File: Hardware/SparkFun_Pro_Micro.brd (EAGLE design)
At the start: 17.8 x 33 mm, 105 parts, among them J2 Qwiic, U1 3.3V, U3 ATmega32U4, Y2 16MHz

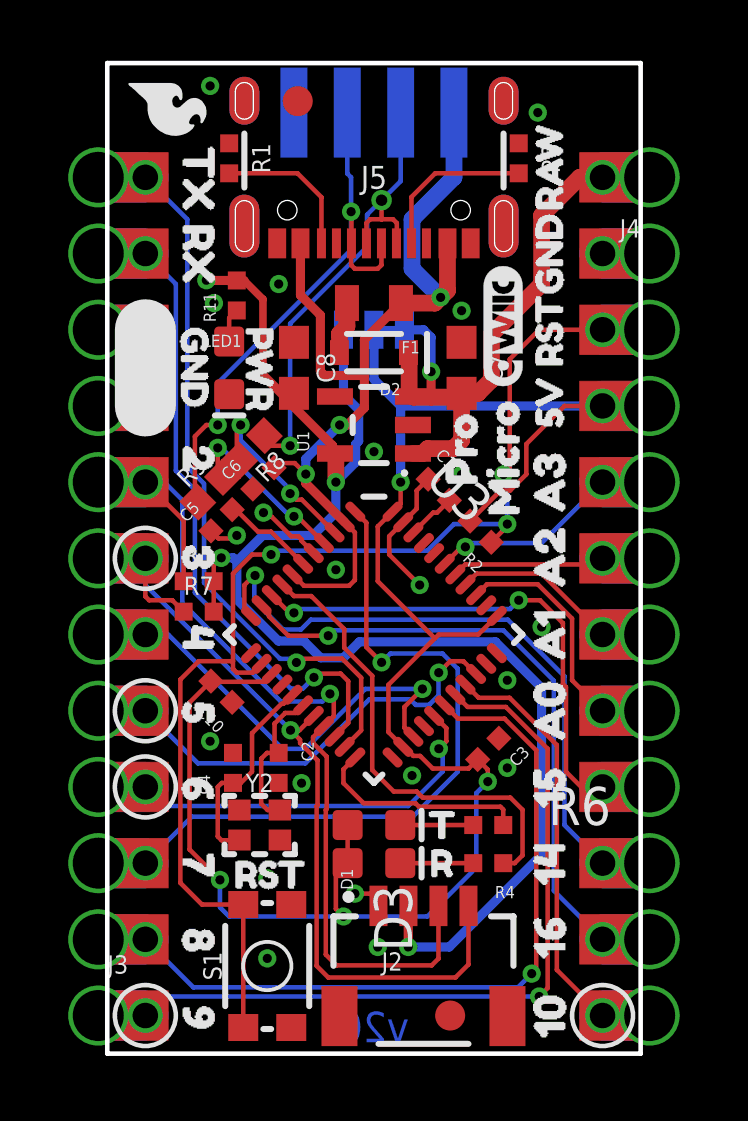
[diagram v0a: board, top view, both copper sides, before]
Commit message: fixing paste issue
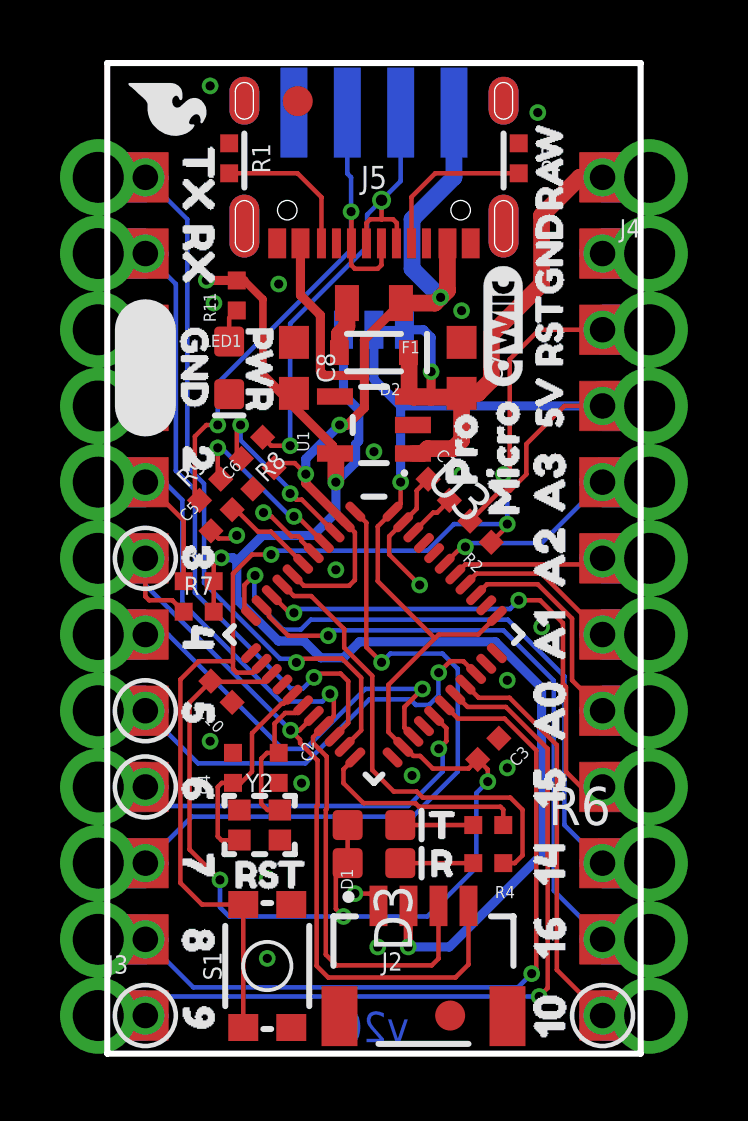
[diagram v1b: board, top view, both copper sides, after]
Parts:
- J2: value Qwiic -> QWIIC_RIGHT_ANGLE
- JP4: value (none) -> JUMPER-SMT_3_1-NC_TRACE_SILK
- R8, R9: value 22 -> 5.1k; device SparkFun-Resistors:0402 -> SparkFun-Resistors:0402-TIGHT
- U3: value ATmega32U4 -> 32U4; device SparkFun-IC-Microcontroller:QFN-44-NOPAD_1:1 -> SparkFun-IC-Microcontroller:QFN-44-NOPAD_1:1-LESS_PASTE
- moved U$32 2.90 mm to (14.7, 24.4), turned to 90 degrees
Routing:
- net RAW: track 19.5 -> 20.4 mm

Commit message: changing PROD_ID on series D+/D- resistor to proper PROD_ID
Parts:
- R8, R9: value 5.1k -> 22OHM-0402T-1/16W-1%
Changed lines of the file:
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@@
 <attribute name="VALUE" x="8.89" y="1.624" size="0.6096" layer="27" font="vector" ratio="20"/>
 </element>
-<element name="R8" library="SparkFun-Resistors" package="0402-TIGHT" value="5.1k" x="4.826" y="20.193" smashed="yes" rot="R225">
+<element name="R8" library="SparkFun-Resistors" package="0402-TIGHT" value="22OHM-0402T-1/16W-1%" x="4.826" y="20.193" smashed="yes" rot="R225">
 <attribute name="NAME" x="5.223396875" y="19.79560625" size="0.6096" layer="25" font="vector" ratio="20" rot="R225" align="bottom-center"/>
-<attribute name="PROD_ID" value="RES-14340" x="4.826" y="20.193" size="1.778" layer="27" font="vector" ratio="15" rot="R225" display="off"/>
-<attribute name="VALUE" value="5.1k" x="4.42860625" y="20.590396875" size="0.6096" layer="27" font="vector" ratio="20" rot="R225" align="top-center"/>
+<attribute name="PROD_ID" value="RES-12427" x="4.826" y="20.193" size="1.778" layer="27" font="vector" ratio="15" rot="R225" display="off"/>
 </element>
-<element name="R9" library="SparkFun-Resistors" package="0402-TIGHT" value="5.1k" x="3.429" y="18.796" smashed="yes" rot="R45">
+<element name="R9" library="SparkFun-Resistors" package="0402-TIGHT" value="22OHM-0402T-1/16W-1%" x="3.429" y="18.796" smashed="yes" rot="R45">
 <attribute name="NAME" x="3.031603125" y="19.19339375" size="0.6096" layer="25" font="vector" ratio="20" rot="R45" align="bottom-center"/>
-<attribute name="PROD_ID" value="RES-14340" x="3.429" y="18.796" size="1.778" layer="27" font="vector" ratio="15" rot="R45" display="off"/>
-<attribute name="VALUE" value="5.1k" x="3.82639375" y="18.398603125" size="0.6096" layer="27" font="vector" ratio="20" rot="R45" align="top-center"/>
+<attribute name="PROD_ID" value="RES-12427" x="3.429" y="18.796" size="1.778" layer="27" font="vector" ratio="15" rot="R45" display="off"/>
 </element>
 <element name="U$13" library="buzzard_labels (13)" package="45" value="" x="3.048" y="15.367" smashed="yes" rot="R270"/>

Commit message: Boogie Board Silk Added
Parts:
- removed LOGO1: SFE_LOGO_NAME_FLAME.1_INCH, SparkFun-Aesthetics:SFE_LOGO_NAME_FLAME_.1
- removed LOGO3: QWIIC_LOGO_6MM, SparkFun-Aesthetics:QWIIC_6MM
- removed U$40: (no value), buzzard_labels (18):C5
- removed U$43: (no value), buzzard_labels (18):MICRO4
- removed U$45: (no value), buzzard_labels (18):PRO3
